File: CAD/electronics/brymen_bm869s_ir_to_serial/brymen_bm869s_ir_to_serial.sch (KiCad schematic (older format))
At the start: 8 parts, among them J1 Conn_01x04_Male, Q1 2N3904, U1 ATtiny85-20PU

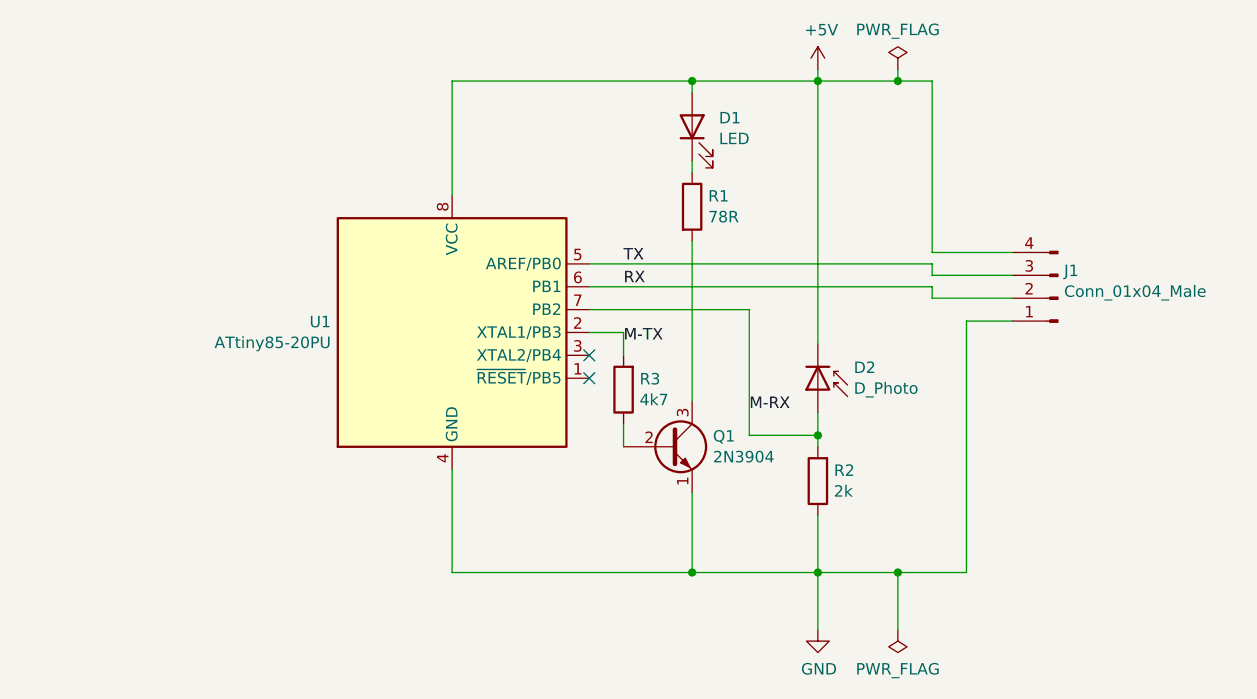
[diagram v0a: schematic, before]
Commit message: Modified code to be work with an attiny84a MCU
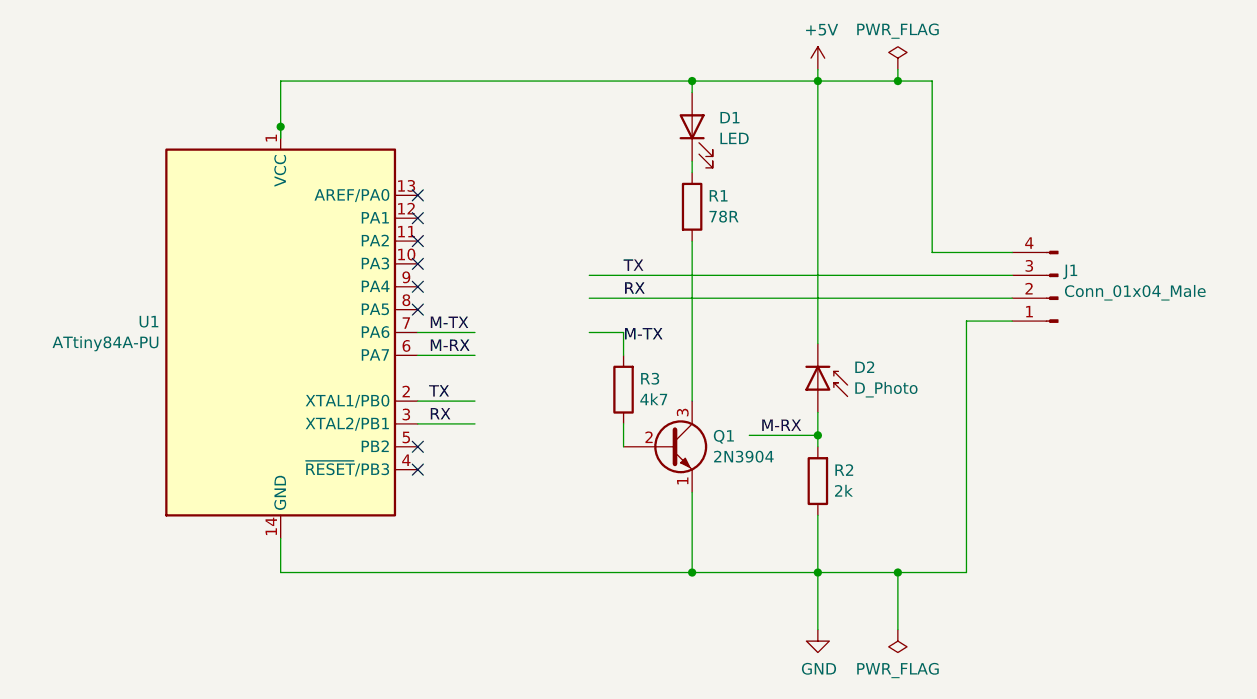
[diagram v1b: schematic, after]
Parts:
- removed U1: ATtiny85-20PU, Package_DIP:DIP-8_W7.62mm, symbol MCU_Microchip_ATtiny:ATtiny85-20PU
- added U1: ATtiny84A-PU, Package_DIP:DIP-14_W7.62mm, symbol MCU_Microchip_ATtiny:ATtiny84A-PU
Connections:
- wire segments 38 -> 37
- no-connect marks 2 -> 8
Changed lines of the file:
@@
 EESchema Schematic File Version 4
-EELAYER 26 0
+EELAYER 30 0
 EELAYER END
 $Descr A4 11693 8268
@@
 $EndComp
 $Comp
-L MCU_Microchip_ATtiny:ATtiny85-20PU U1
-U 1 1 5C0672F2
-P 3400 2150
-F 0 "U1" H 2870 2196 50  0000 R CNN
-F 1 "ATtiny85-20PU" H 2870 2105 50  0000 R CNN
-F 2 "Package_DIP:DIP-8_W7.62mm" H 3400 2150 50  0001 C CIN
-F 3 "http://ww1.microchip.com/downloads/en/DeviceDoc/atmel-2586-avr-8-bit-microcontroller-attiny25-attiny45-attiny85_datasheet.pdf" H 3400 2150 50  0001 C CNN
-	1    3400 2150
-	1    0    0    -1
-$EndComp
-$Comp
 L power:+5V #PWR01
 U 1 1 5C0673A0
@@
 $EndComp
 Wire Wire Line
-	4000 1850 5500 1850
-Wire Wire Line
-	5500 1850 5500 1900
-Wire Wire Line
-	5500 1900 5850 1900
-Wire Wire Line
-	4000 1950 5500 1950
-Wire Wire Line
-	5500 1950 5500 2000
-Wire Wire Line
-	5500 2000 5850 2000
-NoConn ~ 4000 2250
-NoConn ~ 4000 2350
-Wire Wire Line
 	5000 2500 5000 2600
 Wire Wire Line
@@
 Wire Wire Line
 	5650 3200 5350 3200
-Wire Wire Line
-	3400 3200 3400 2750
 Wire Wire Line
 	5000 2950 5000 3200
@@
 	4150 2150 4000 2150
 Wire Wire Line
-	4000 2050 4700 2050
-Wire Wire Line
-	4700 2050 4700 2600
-Wire Wire Line
 	4700 2600 5000 2600
 Connection ~ 5000 2600
@@
 Wire Wire Line
 	5350 3200 5000 3200
-Text Label 4150 1850 0    50   ~ 0
-TX
-Text Label 4150 1950 0    50   ~ 0
-RX
 Text Label 4150 2200 0    50   ~ 0
 M-TX
-Text Label 4700 2500 0    50   ~ 0
+Text Label 4750 2600 0    50   ~ 0
 M-RX
 $Comp
@@
 	4150 2550 4150 2650
 Wire Wire Line
-	3400 3200 4450 3200
-Wire Wire Line
 	5850 1800 5500 1800
 Wire Wire Line
@@
 Wire Wire Line
 	5500 1050 5350 1050
-Wire Wire Line
-	3400 1050 3400 1550
 Wire Wire Line
 	5000 1000 5000 1050
@@
 Connection ~ 4450 1050
 Wire Wire Line
-	4450 1050 3400 1050
-Wire Wire Line
 	4450 1400 4450 1450
 Wire Wire Line
@@
 Wire Wire Line
 	4450 3200 5000 3200
+$Comp
+L MCU_Microchip_ATtiny:ATtiny84A-PU U1
+U 1 1 5F481036
+P 2650 2150
+F 0 "U1" H 2121 2196 50  0000 R CNN
+F 1 "ATtiny84A-PU" H 2121 2105 50  0000 R CNN
+F 2 "Package_DIP:DIP-14_W7.62mm" H 2650 2150 50  0001 C CIN
+F 3 "http://ww1.microchip.com/downloads/en/DeviceDoc/doc8183.pdf" H 2650 2150 50  0001 C CNN
+	1    2650 2150
+	1    0    0    -1
+$EndComp
+Wire Wire Line
+	2650 1050 2650 1250
+Wire Wire Line
+	2650 1050 4450 1050
+Wire Wire Line
+	2650 3200 4450 3200
+Connection ~ 2650 1250
+Wire Wire Line
+	2650 1250 2650 1300
+Wire Wire Line
+	3250 2250 3500 2250
+Wire Wire Line
+	3250 2150 3500 2150
+Text Label 3300 2150 0    50   ~ 0
+M-TX
+Text Label 3300 2250 0    50   ~ 0
+M-RX
+Wire Wire Line
+	3250 2450 3500 2450
+Wire Wire Line
+	3250 2550 3500 2550
+Text Label 3300 2450 0    50   ~ 0
+TX
+Text Label 3300 2550 0    50   ~ 0
+RX
+Text Label 4150 1900 0    50   ~ 0
+TX
+Text Label 4150 2000 0    50   ~ 0
+RX
+Wire Wire Line
+	4000 2000 5850 2000
+Wire Wire Line
+	4000 1900 5850 1900
+NoConn ~ 3250 1550
+NoConn ~ 3250 1650
+NoConn ~ 3250 1750
+NoConn ~ 3250 1850
+NoConn ~ 3250 1950
+NoConn ~ 3250 2050
+NoConn ~ 3250 2650
+NoConn ~ 3250 2750
+Wire Wire Line
+	2650 3050 2650 3200
 $EndSCHEMATC

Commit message: Added a PCB design, but it has not been verified.
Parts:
- D1, D2: footprint (none) -> LED_THT:LED_D4.0mm
- J1: footprint (none) -> Connector_PinHeader_2.54mm:PinHeader_1x04_P2.54mm_Vertical
- Q1: footprint Package_TO_SOT_THT:TO-92_Inline -> Package_TO_SOT_SMD:SOT-23
- R1, R2, R3: footprint (none) -> Resistor_SMD:R_0603_1608Metric
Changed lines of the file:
@@
 F 0 "D1" V 4488 1133 50  0000 R CNN
 F 1 "LED" V 4397 1133 50  0000 R CNN
-F 2 "" H 4450 1250 50  0001 C CNN
+F 2 "LED_THT:LED_D4.0mm" H 4450 1250 50  0001 C CNN
 F 3 "~" H 4450 1250 50  0001 C CNN
 	1    4450 1250
@@
 F 0 "J1" H 6023 1880 50  0000 R CNN
 F 1 "Conn_01x04_Male" H 6023 1971 50  0000 R CNN
-F 2 "" H 6050 2000 50  0001 C CNN
+F 2 "Connector_PinHeader_2.54mm:PinHeader_1x04_P2.54mm_Vertical" H 6050 2000 50  0001 C CNN
 F 3 "~" H 6050 2000 50  0001 C CNN
 	1    6050 2000
@@
 F 0 "R1" H 4520 1646 50  0000 L CNN
 F 1 "78R" H 4520 1555 50  0000 L CNN
-F 2 "" V 4380 1600 50  0001 C CNN
+F 2 "Resistor_SMD:R_0603_1608Metric" V 4380 1600 50  0001 C CNN
 F 3 "~" H 4450 1600 50  0001 C CNN
 	1    4450 1600
@@
 F 0 "D2" V 4904 2557 50  0000 L CNN
 F 1 "D_Photo" V 4995 2557 50  0000 L CNN
-F 2 "" H 4950 2400 50  0001 C CNN
+F 2 "LED_THT:LED_D4.0mm" H 4950 2400 50  0001 C CNN
 F 3 "~" H 4950 2400 50  0001 C CNN
 	1    5000 2400
@@
 F 0 "R2" H 4930 2754 50  0000 R CNN
 F 1 "2k" H 4930 2845 50  0000 R CNN
-F 2 "" V 4930 2800 50  0001 C CNN
+F 2 "Resistor_SMD:R_0603_1608Metric" V 4930 2800 50  0001 C CNN
 F 3 "~" H 5000 2800 50  0001 C CNN
 	1    5000 2800
@@
 F 0 "Q1" H 4541 2696 50  0000 L CNN
 F 1 "2N3904" H 4541 2605 50  0000 L CNN
-F 2 "Package_TO_SOT_THT:TO-92_Inline" H 4550 2575 50  0001 L CIN
+F 2 "Package_TO_SOT_SMD:SOT-23" H 4550 2575 50  0001 L CIN
 F 3 "https://www.fairchildsemi.com/datasheets/2N/2N3904.pdf" H 4350 2650 50  0001 L CNN
 	1    4350 2650
@@
 F 0 "R3" H 4080 2354 50  0000 R CNN
 F 1 "4k7" H 4080 2445 50  0000 R CNN
-F 2 "" V 4080 2400 50  0001 C CNN
+F 2 "Resistor_SMD:R_0603_1608Metric" V 4080 2400 50  0001 C CNN
 F 3 "~" H 4150 2400 50  0001 C CNN
 	1    4150 2400

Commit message: changes...?
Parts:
- removed Q1: 2N3904, Package_TO_SOT_SMD:SOT-23, symbol Transistor_BJT:2N3904
- added Q1: BC817, TO_SOT_Packages_SMD:SOT-23, symbol Transistor_BJT:BC817
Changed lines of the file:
@@
 M-RX
-$Comp
-L Transistor_BJT:2N3904 Q1
-U 1 1 5C06A9ED
-P 4350 2650
-F 0 "Q1" H 4541 2696 50  0000 L CNN
-F 1 "2N3904" H 4541 2605 50  0000 L CNN
-F 2 "Package_TO_SOT_SMD:SOT-23" H 4550 2575 50  0001 L CIN
-F 3 "https://www.fairchildsemi.com/datasheets/2N/2N3904.pdf" H 4350 2650 50  0001 L CNN
-	1    4350 2650
-	1    0    0    -1
-$EndComp
 $Comp
 L Device:R R3
@@
 	-1   0    0    1
 $EndComp
-Wire Wire Line
-	4150 2550 4150 2650
 Wire Wire Line
 	5850 1800 5500 1800
@@
 Wire Wire Line
 	4450 1750 4450 2450
-Wire Wire Line
-	4450 2850 4450 3200
-Connection ~ 4450 3200
-Wire Wire Line
-	4450 3200 5000 3200
 $Comp
 L MCU_Microchip_ATtiny:ATtiny84A-PU U1
@@
 Wire Wire Line
 	2650 1050 4450 1050
-Wire Wire Line
-	2650 3200 4450 3200
 Connection ~ 2650 1250
 Wire Wire Line
@@
 Wire Wire Line
 	2650 3050 2650 3200
+$Comp
+L Transistor_BJT:BC817 Q1
+U 1 1 5F4C2395
+P 4350 2650
+F 0 "Q1" H 4541 2696 50  0000 L CNN
+F 1 "BC817" H 4541 2605 50  0000 L CNN
+F 2 "TO_SOT_Packages_SMD:SOT-23" H 4550 2575 50  0001 L CIN
+F 3 "http://www.fairchildsemi.com/ds/BC/BC817.pdf" H 4350 2650 50  0001 L CNN
+	1    4350 2650
+	1    0    0    -1
+$EndComp
+Wire Wire Line
+	2650 3200 4450 3200
+Wire Wire Line
+	4450 2850 4450 3200
+Connection ~ 4450 3200
+Wire Wire Line
+	4450 3200 5000 3200
+Wire Wire Line
+	4150 2650 4150 2550
 $EndSCHEMATC
